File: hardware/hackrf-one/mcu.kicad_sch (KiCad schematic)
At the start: 131 parts, among them J1 USB-MICRO-B, P20 GPIO, P22 I2S, P23 DBGEN, P24 TRST, P25 LPC_ISP, P26 LPC_JTAG, P28 SD, P29 CPLD_JTAG, P3 GND, P30 BANK2_AUX, P5 LEDS, P68 SPIFI_CS, P69 VREGMODE, P70 EN_1V8, P71 ID, P73 P1_2, P74 P1_1, P75 GP_CLKIN, P76 GP_CLKIN, P77 GP_CLKIN, P78 GP_CLKIN, P79 GP_CLKIN, P80 SHIELD, P81 SPIFI_SIO2, P82 SPIFI_SIO3, Q5 MOSFET_P, SW1 DFU, SW2 RESET, U15 TVS, U20 W25Q80, U21 TPS62410, U23 LPC4320FBD144, U24 GSG-XC2C64A-7VQG100C, X2 MCU_XTAL, X3 RTC_XTAL

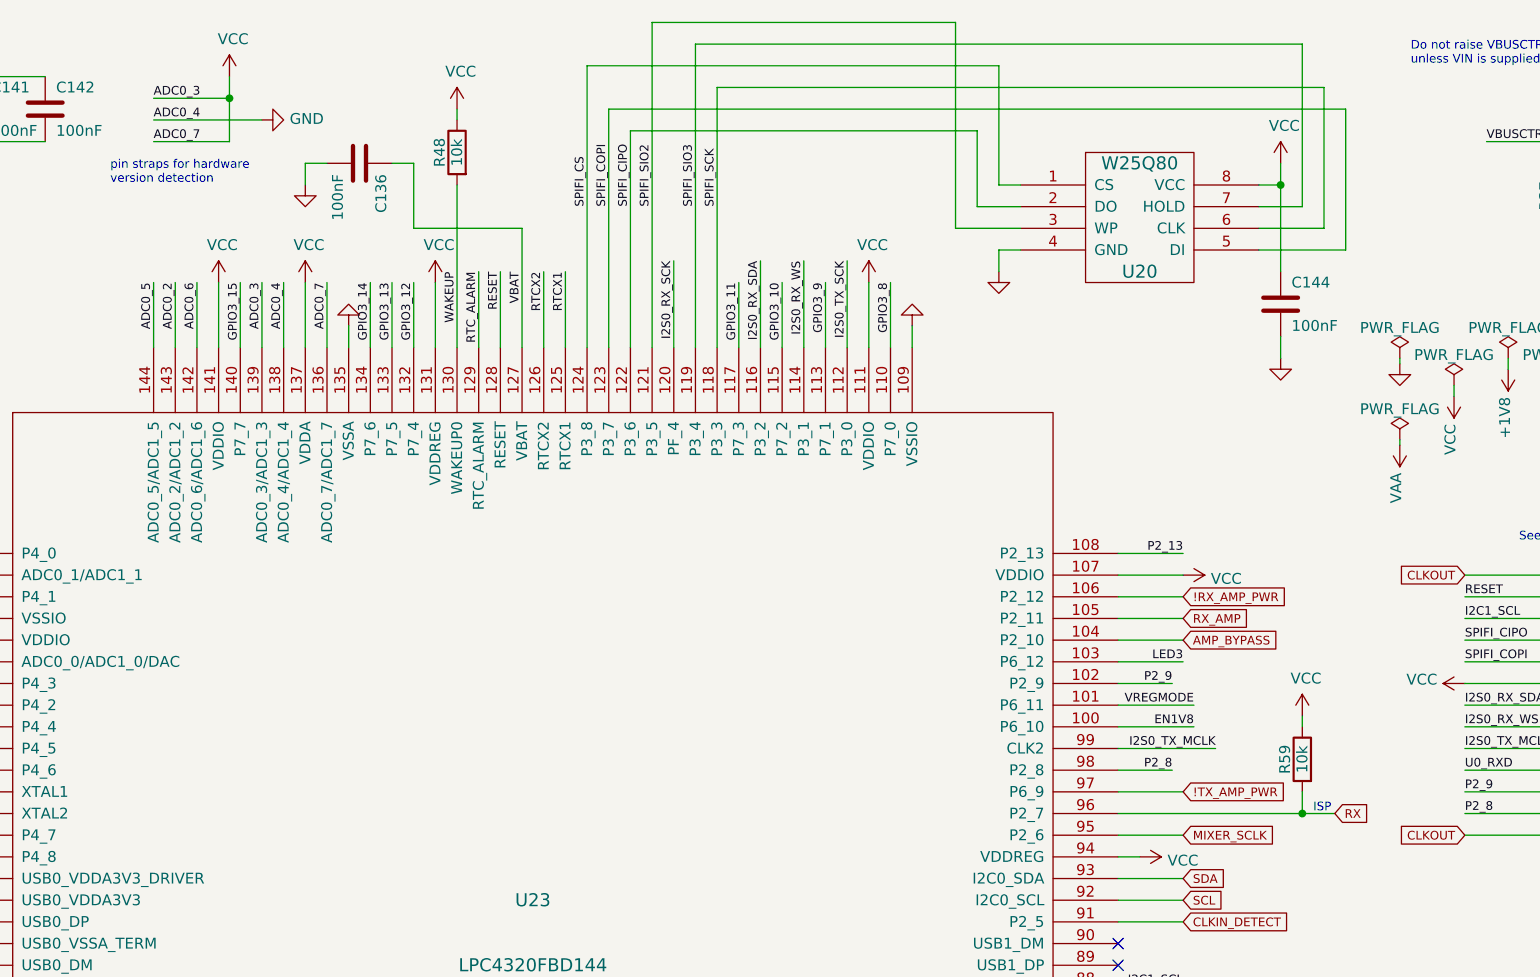
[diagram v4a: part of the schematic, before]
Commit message: HackRF One: update hardware detection pin straps
Additionally swap:
 - EN_1V8, P6_10, U23 pin 100 (pull-down)
 - !RX_AMP_PWR, P2_12, U23 pin 106 (pull-up)

Detecting which has the pull-up and which has the pull-down enables
version detection that may be more reliable than the ADC method.
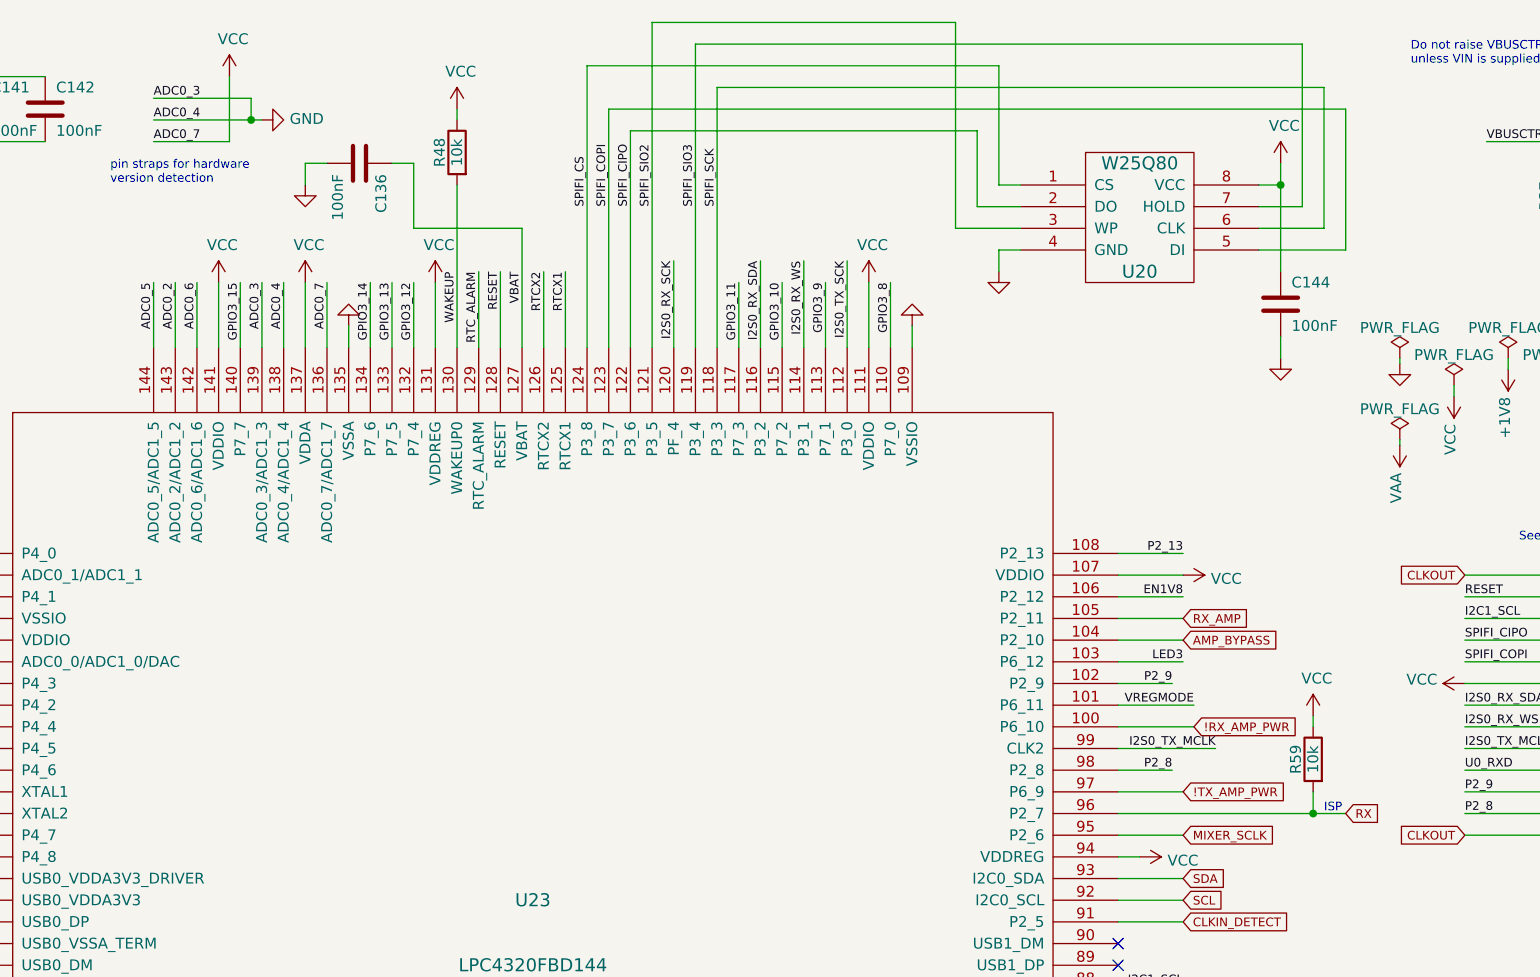
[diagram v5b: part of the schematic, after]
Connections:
- net !RX_AMP_PWR: now also U23.100 (P6_10); no longer U23.106 (P2_12)
- net EN1V8: now also U23.106 (P2_12); no longer U23.100 (P6_10)
- net GND: now also U23.139 (ADC0_3/ADC1_3)
- net VCC: no longer U23.139 (ADC0_3/ADC1_3)
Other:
- moved on the sheet: R59
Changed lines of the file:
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@@
   (junction (at 344.17 68.58) (diameter 0) (color 0 0 0 0)
   )
-  (junction (at 267.97 106.68) (diameter 0) (color 0 0 0 0)
+  (junction (at 269.24 106.68) (diameter 0) (color 0 0 0 0)
   )
   (junction (at 90.17 27.94) (diameter 0) (color 0 0 0 0)
@@
   (junction (at 82.55 27.94) (diameter 0) (color 0 0 0 0)
   )
+  (junction (at 144.78 25.4) (diameter 0) (color 0 0 0 0)
+  )
   (junction (at 372.11 17.78) (diameter 0) (color 0 0 0 0)
   )
@@
   (junction (at 356.87 106.68) (diameter 0) (color 0 0 0 0)
   )
-  (junction (at 142.24 22.86) (diameter 0) (color 0 0 0 0)
-  )
   (junction (at 391.16 99.06) (diameter 0) (color 0 0 0 0)
   )
@@
     (stroke (width 0) (type default) (color 0 0 0 0))
   )
-  (wire (pts (xy 142.24 22.86) (xy 142.24 20.32))
+  (wire (pts (xy 142.24 20.32) (xy 142.24 27.94))
+    (stroke (width 0) (type default) (color 0 0 0 0))
+  )
+  (wire (pts (xy 133.35 22.86) (xy 144.78 22.86))
     (stroke (width 0) (type default) (color 0 0 0 0))
   )
@@
     (stroke (width 0) (type default) (color 0 0 0 0))
   )
-  (wire (pts (xy 246.38 106.68) (xy 267.97 106.68))
+  (wire (pts (xy 246.38 106.68) (xy 269.24 106.68))
     (stroke (width 0) (type default) (color 0 0 0 0))
   )
@@
     (stroke (width 0) (type default) (color 0 0 0 0))
   )
-  (wire (pts (xy 267.97 106.68) (xy 271.78 106.68))
+  (wire (pts (xy 269.24 106.68) (xy 273.05 106.68))
     (stroke (width 0) (type default) (color 0 0 0 0))
   )
@@
     (stroke (width 0) (type default) (color 0 0 0 0))
   )
-  (wire (pts (xy 267.97 95.25) (xy 267.97 96.52))
+  (wire (pts (xy 269.24 95.25) (xy 269.24 96.52))
     (stroke (width 0) (type default) (color 0 0 0 0))
   )
@@
     (stroke (width 0) (type default) (color 0 0 0 0))
   )
-  (wire (pts (xy 133.35 22.86) (xy 142.24 22.86))
-    (stroke (width 0) (type default) (color 0 0 0 0))
-  )
   (wire (pts (xy 109.22 78.74) (xy 106.68 78.74))
     (stroke (width 0) (type default) (color 0 0 0 0))
@@
     (stroke (width 0) (type default) (color 0 0 0 0))
   )
-  (wire (pts (xy 133.35 25.4) (xy 146.05 25.4))
+  (wire (pts (xy 133.35 25.4) (xy 144.78 25.4))
     (stroke (width 0) (type default) (color 0 0 0 0))
   )
@@
     (stroke (width 0) (type default) (color 0 0 0 0))
   )
+  (wire (pts (xy 144.78 22.86) (xy 144.78 25.4))
+    (stroke (width 0) (type default) (color 0 0 0 0))
+  )
   (wire (pts (xy 196.85 16.51) (xy 267.97 16.51))
     (stroke (width 0) (type default) (color 0 0 0 0))
@@
     (stroke (width 0) (type default) (color 0 0 0 0))
   )
+  (wire (pts (xy 144.78 25.4) (xy 146.05 25.4))
+    (stroke (width 0) (type default) (color 0 0 0 0))
+  )
   (wire (pts (xy 246.38 134.62) (xy 254 134.62))
     (stroke (width 0) (type default) (color 0 0 0 0))
@@
     (stroke (width 0) (type default) (color 0 0 0 0))
   )
-  (wire (pts (xy 267.97 104.14) (xy 267.97 106.68))
+  (wire (pts (xy 269.24 104.14) (xy 269.24 106.68))
     (stroke (width 0) (type default) (color 0 0 0 0))
   )
@@
     (stroke (width 0) (type default) (color 0 0 0 0))
   )
-  (wire (pts (xy 142.24 22.86) (xy 142.24 27.94))
-    (stroke (width 0) (type default) (color 0 0 0 0))
-  )
   (wire (pts (xy 45.72 90.17) (xy 86.36 90.17))
     (stroke (width 0) (type default) (color 0 0 0 0))
@@
     (effects (font (size 1.016 1.016)) (justify left bottom))
   )
-  (text "ISP" (at 269.24 106.68 0)
+  (text "ISP" (at 270.51 106.68 0)
     (effects (font (size 1.016 1.016)) (justify left bottom))
   )
@@
     (effects (font (size 1.016 1.016)) (justify right bottom))
   )
-  (label "EN1V8" (at 255.27 96.52 180)
+  (label "EN1V8" (at 254 81.28 180)
     (effects (font (size 1.016 1.016)) (justify right bottom))
   )
@@
     (effects (font (size 1.016 1.016)) (justify left bottom))
   )
-  (global_label "!RX_AMP_PWR" (shape input) (at 254 81.28 0) (fields_autoplaced)
+  (global_label "!RX_AMP_PWR" (shape input) (at 255.27 96.52 0) (fields_autoplaced)
     (effects (font (size 1.016 1.016)) (justify left))
-    (property "Intersheet References" "${INTERSHEET_REFS}" (id 0) (at 0 0 0)
+    (property "Intersheet References" "${INTERSHEET_REFS}" (id 0) (at 1.27 15.24 0)
       (effects (font (size 1.27 1.27)) hide)
     )
@@
     )
   )
-  (global_label "RX" (shape input) (at 271.78 106.68 0) (fields_autoplaced)
+  (global_label "RX" (shape input) (at 273.05 106.68 0) (fields_autoplaced)
     (effects (font (size 1.016 1.016)) (justify left))
-    (property "Intersheet References" "${INTERSHEET_REFS}" (id 0) (at 17.78 -12.7 0)
+    (property "Intersheet References" "${INTERSHEET_REFS}" (id 0) (at 19.05 -12.7 0)
       (effects (font (size 1.27 1.27)) hide)
     )
@@
     (pin "2")
   )
-  (symbol (lib_id "Device:R") (at 267.97 100.33 0) (mirror y) (unit 1)
+  (symbol (lib_id "Device:R") (at 269.24 100.33 0) (mirror y) (unit 1)
     (in_bom yes) (on_board yes)
-    (property "Reference" "R59" (id 0) (at 265.938 100.33 90))
-    (property "Value" "10k" (id 1) (at 267.97 100.33 90))
-    (property "Footprint" "hackrf:GSG-0402" (id 2) (at 267.97 100.33 0)
+    (property "Reference" "R59" (id 0) (at 267.208 100.33 90))
+    (property "Value" "10k" (id 1) (at 269.24 100.33 90))
+    (property "Footprint" "hackrf:GSG-0402" (id 2) (at 269.24 100.33 0)
       (effects (font (size 1.524 1.524)) hide)
     )
-    (property "Datasheet" "" (id 3) (at 267.97 100.33 0)
+    (property "Datasheet" "" (id 3) (at 269.24 100.33 0)
       (effects (font (size 1.524 1.524)) hide)
     )
-    (property "Manufacturer" "Stackpole" (id 4) (at 267.97 100.33 0)
+    (property "Manufacturer" "Stackpole" (id 4) (at 269.24 100.33 0)
       (effects (font (size 1.524 1.524)) hide)
     )
-    (property "Part Number" "RMCF0402JT10K0" (id 5) (at 267.97 100.33 0)
+    (property "Part Number" "RMCF0402JT10K0" (id 5) (at 269.24 100.33 0)
       (effects (font (size 1.524 1.524)) hide)
     )
-    (property "Description" "RES 10K OHM 1/16W 5% 0402 SMD" (id 6) (at 267.97 100.33 0)
+    (property "Description" "RES 10K OHM 1/16W 5% 0402 SMD" (id 6) (at 269.24 100.33 0)
       (effects (font (size 1.524 1.524)) hide)
     )
@@
     (pin "1")
   )
-  (symbol (lib_id "power:VCC") (at 267.97 95.25 0) (unit 1)
+  (symbol (lib_id "power:VCC") (at 269.24 95.25 0) (unit 1)
     (in_bom yes) (on_board yes)
-    (property "Reference" "#PWR0269" (id 0) (at 267.97 99.06 0)
+    (property "Reference" "#PWR0269" (id 0) (at 269.24 99.06 0)
       (effects (font (size 1.27 1.27)) hide)
     )
-    (property "Value" "VCC" (id 1) (at 268.4018 90.8558 0))
-    (property "Footprint" "" (id 2) (at 267.97 95.25 0)
+    (property "Value" "VCC" (id 1) (at 269.6718 90.8558 0))
+    (property "Footprint" "" (id 2) (at 269.24 95.25 0)
       (effects (font (size 1.27 1.27)) hide)
     )
-    (property "Datasheet" "" (id 3) (at 267.97 95.25 0)
+    (property "Datasheet" "" (id 3) (at 269.24 95.25 0)
       (effects (font (size 1.27 1.27)) hide)
     )

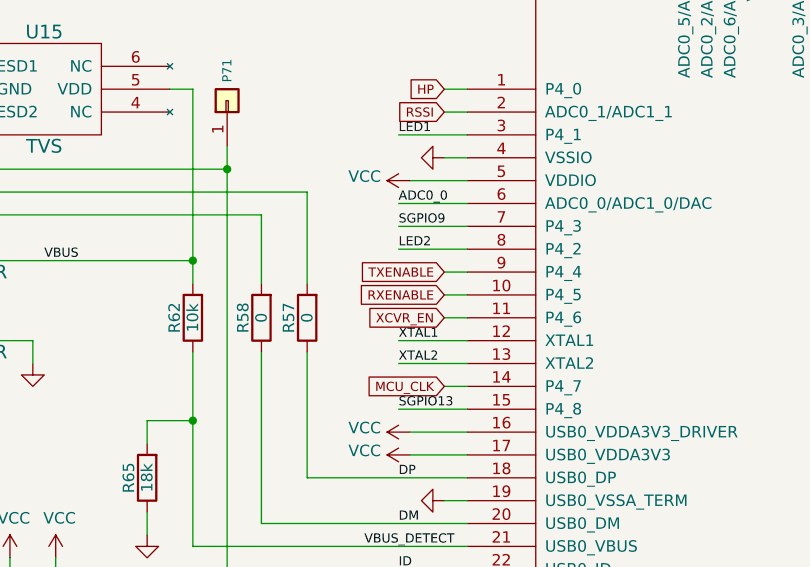
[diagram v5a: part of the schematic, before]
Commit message: HackRF One: change U17 from MAX2837 to MAX2839
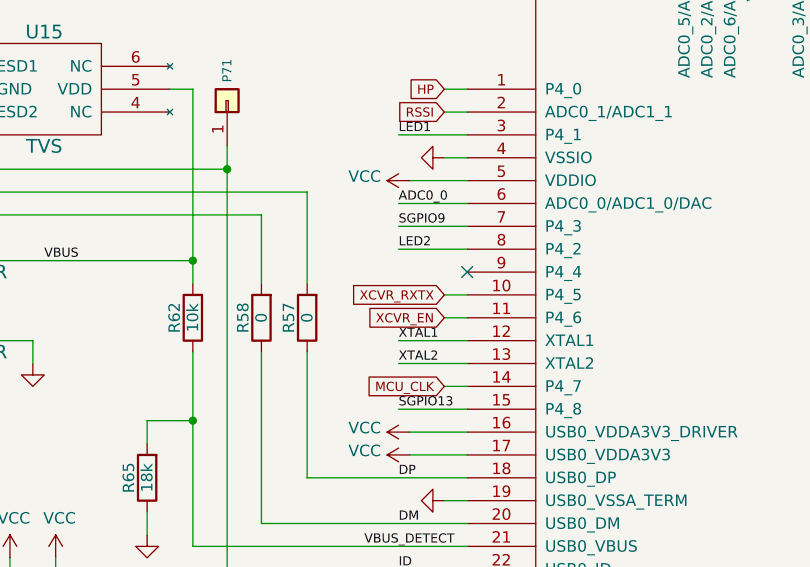
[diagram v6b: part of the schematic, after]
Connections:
- net RXENABLE renamed XCVR_RXTX
- net TXENABLE: no longer names the net of U23.9 (P4_4)
- no-connect marks 14 -> 15
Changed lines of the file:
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@@
   (no_connect (at 396.24 184.15))
   (no_connect (at 294.64 181.61))
+  (no_connect (at 109.22 96.52))
   (no_connect (at 54.61 46.99))
   (no_connect (at 294.64 184.15))
@@
     (stroke (width 0) (type default) (color 0 0 0 0))
   )
-  (wire (pts (xy 109.22 96.52) (xy 106.68 96.52))
-    (stroke (width 0) (type default) (color 0 0 0 0))
-  )
   (wire (pts (xy 25.4 171.45) (xy 25.4 173.99))
     (stroke (width 0) (type default) (color 0 0 0 0))
@@
     )
   )
-  (global_label "RXENABLE" (shape input) (at 106.68 99.06 180) (fields_autoplaced)
-    (effects (font (size 1.016 1.016)) (justify right))
-    (property "Intersheet References" "${INTERSHEET_REFS}" (id 0) (at 0 0 0)
-      (effects (font (size 1.27 1.27)) hide)
-    )
-  )
   (global_label "SCL" (shape input) (at 322.58 109.22 0) (fields_autoplaced)
     (effects (font (size 1.016 1.016)) (justify left))
@@
     )
   )
-  (global_label "TXENABLE" (shape input) (at 106.68 96.52 180) (fields_autoplaced)
+  (global_label "XCVR_RXTX" (shape input) (at 106.68 99.06 180) (fields_autoplaced)
     (effects (font (size 1.016 1.016)) (justify right))
-    (property "Intersheet References" "${INTERSHEET_REFS}" (id 0) (at 0 0 0)
-      (effects (font (size 1.27 1.27)) hide)
+    (property "Intersheet References" "${INTERSHEET_REFS}" (id 0) (at 96.4508 99.1235 0)
+      (effects (font (size 1.016 1.016)) (justify right) hide)
     )
   )

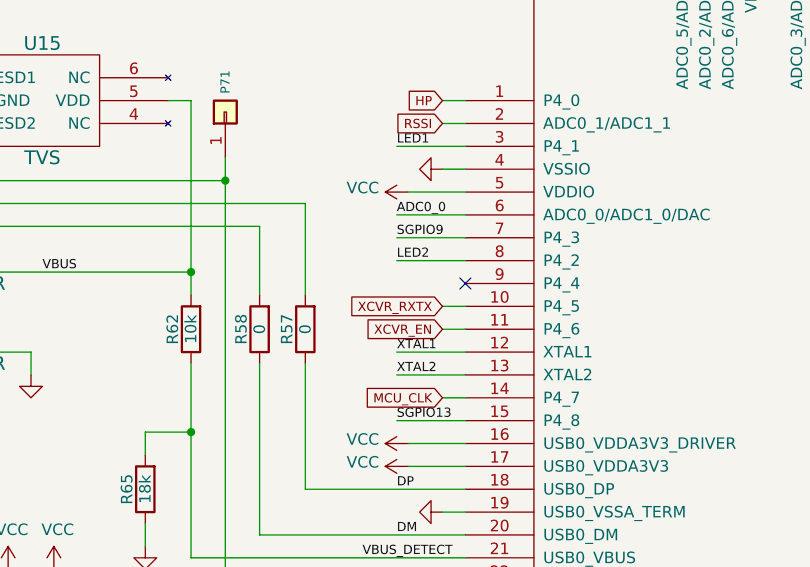
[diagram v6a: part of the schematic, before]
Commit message: HackRF One: move !ANT_BIAS control from U4 to U23
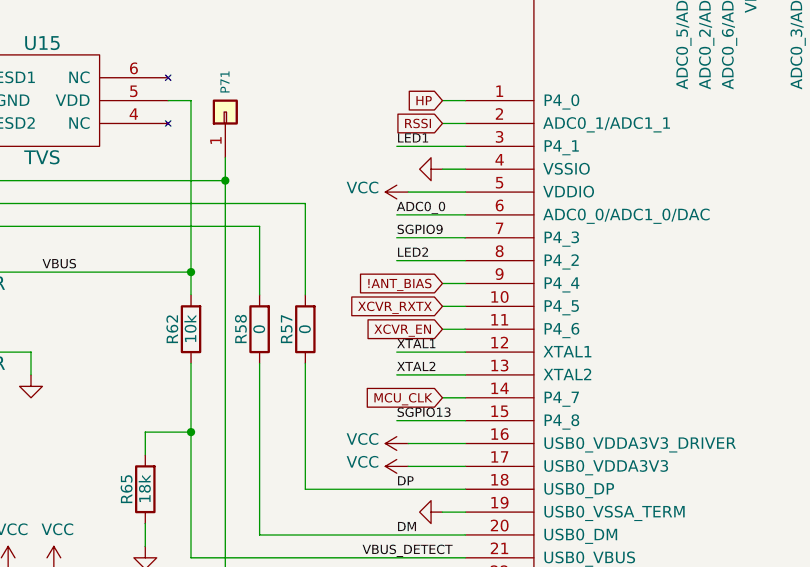
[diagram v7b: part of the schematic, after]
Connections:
- net !ANT_BIAS: now reaches U23.9 (P4_4)
- no-connect marks 15 -> 14
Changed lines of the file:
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@@
   (no_connect (at 396.24 184.15))
   (no_connect (at 294.64 181.61))
-  (no_connect (at 109.22 96.52))
   (no_connect (at 54.61 46.99))
   (no_connect (at 294.64 184.15))
@@
     (stroke (width 0) (type default) (color 0 0 0 0))
   )
+  (wire (pts (xy 106.68 96.52) (xy 109.22 96.52))
+    (stroke (width 0) (type default) (color 0 0 0 0))
+  )
   (wire (pts (xy 93.98 134.62) (xy 109.22 134.62))
     (stroke (width 0) (type default) (color 0 0 0 0))
@@
       (effects (font (size 1.016 1.016)) (justify right) hide)
     )
+  )
+  (global_label "!ANT_BIAS" (shape input) (at 106.68 96.52 180) (fields_autoplaced)
+    (effects (font (size 1.016 1.016)) (justify right))
+    (property "Intersheet References" "${INTERSHEET_REFS}" (id 0) (at 97.5152 96.5835 0)
+      (effects (font (size 1.016 1.016)) (justify right) hide)
+    )

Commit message: HackRF One: component selections, DNP, and Notes
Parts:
- C118, C157, C158, C164: Manufacturer Murata -> Samsung; Part Number GRM1555C1H180JA01D -> CL05C180JB5NNNC
- C125: Manufacturer Murata -> Samsung; Part Number GRM1555C1H330JA01D -> CL05C330JB5NNNC
- C126, C127, C143, C145, C146: Manufacturer Murata -> Samsung; Part Number GRM21BR61A106KE19L -> CL21A106KOQNNNE
- C155, NT1, NT2, P23, P24, P25, P26, P29, P3, P30, P5, P68, P69, P70, P71, P73, P74, P75, P76, P77, P78, P79, P80, P81, P82, R35: DNP (none) -> DNP; Note DNP -> (none)
- L10, L11: Part Number NRG4026T4R7M -> NRS4018T4R7MDGJ
- Q5: Manufacturer Alpha and Omega -> Yangzhou Yangjie; Part Number AO3407A -> YJL2301C
- R69: Manufacturer Rohm -> Yageo; Part Number MCR01MRTF1202 -> RC0402FR-0712KL
